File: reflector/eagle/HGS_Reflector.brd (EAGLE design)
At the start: 100 x 100 mm, 27 parts, among them J1 U.FL, U3 LP2985XX-N

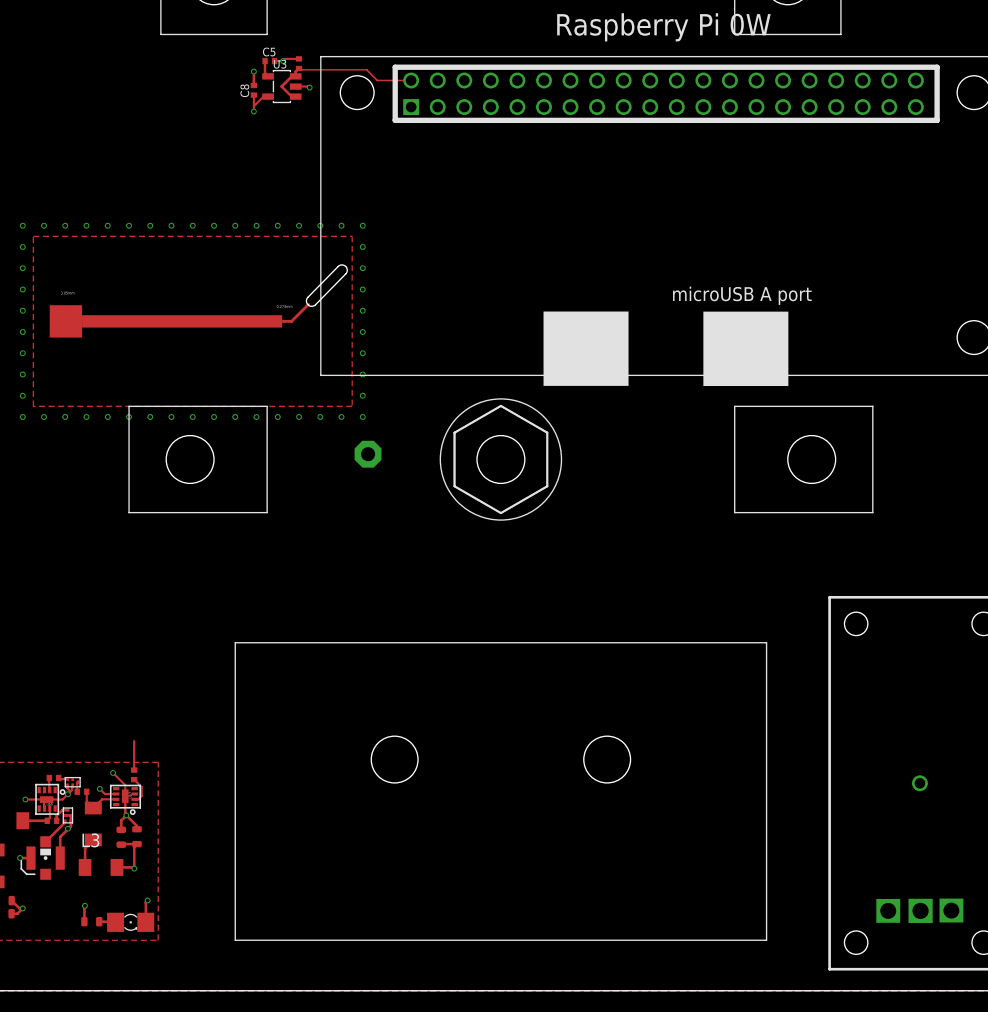
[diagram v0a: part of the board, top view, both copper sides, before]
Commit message: After connecting the Pi 0W footprint to the ground plane, I fixed the issue of the Pi 0W pin header floating.
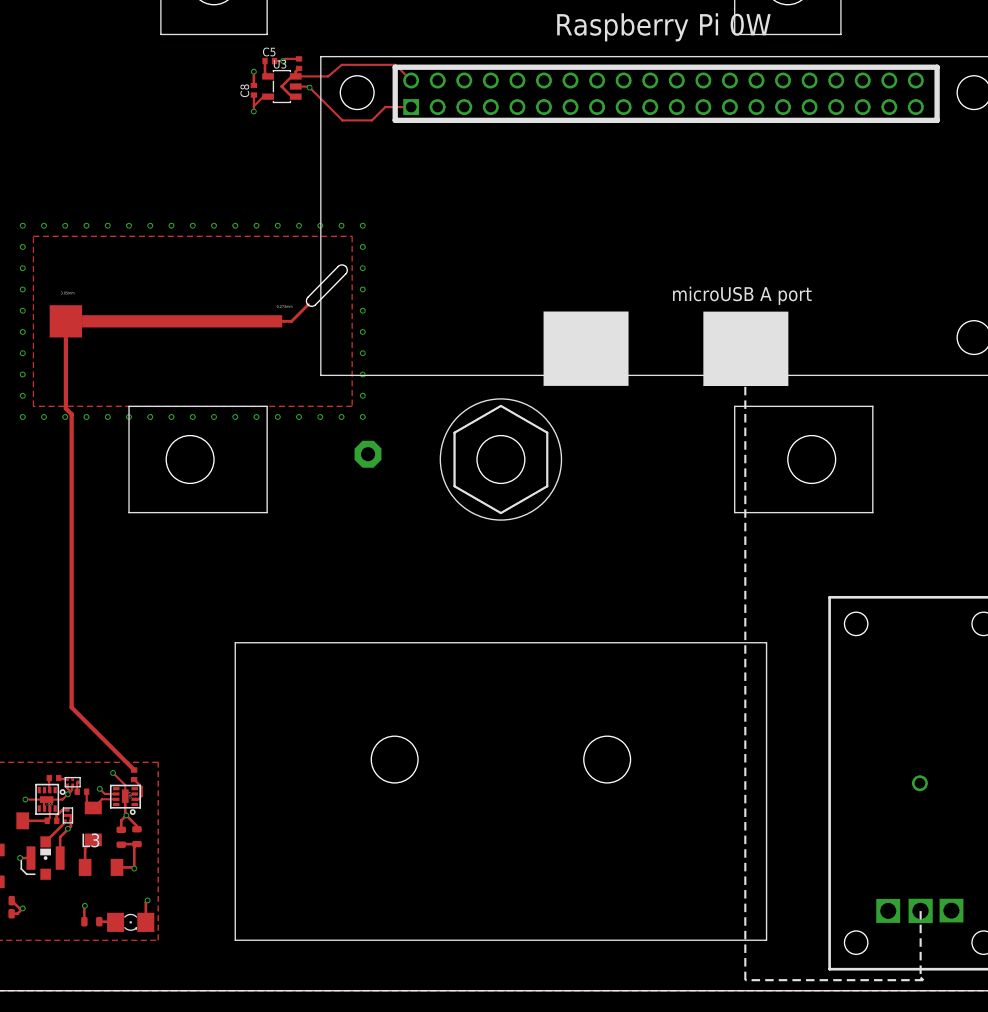
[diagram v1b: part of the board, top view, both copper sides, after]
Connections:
- net GND: now also U$5.GND
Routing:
- net N$9: track 2.73 -> 44.9 mm
- net GND: track 32.1 -> 43.5 mm
- net N$15: track 15.3 -> 16.2 mm

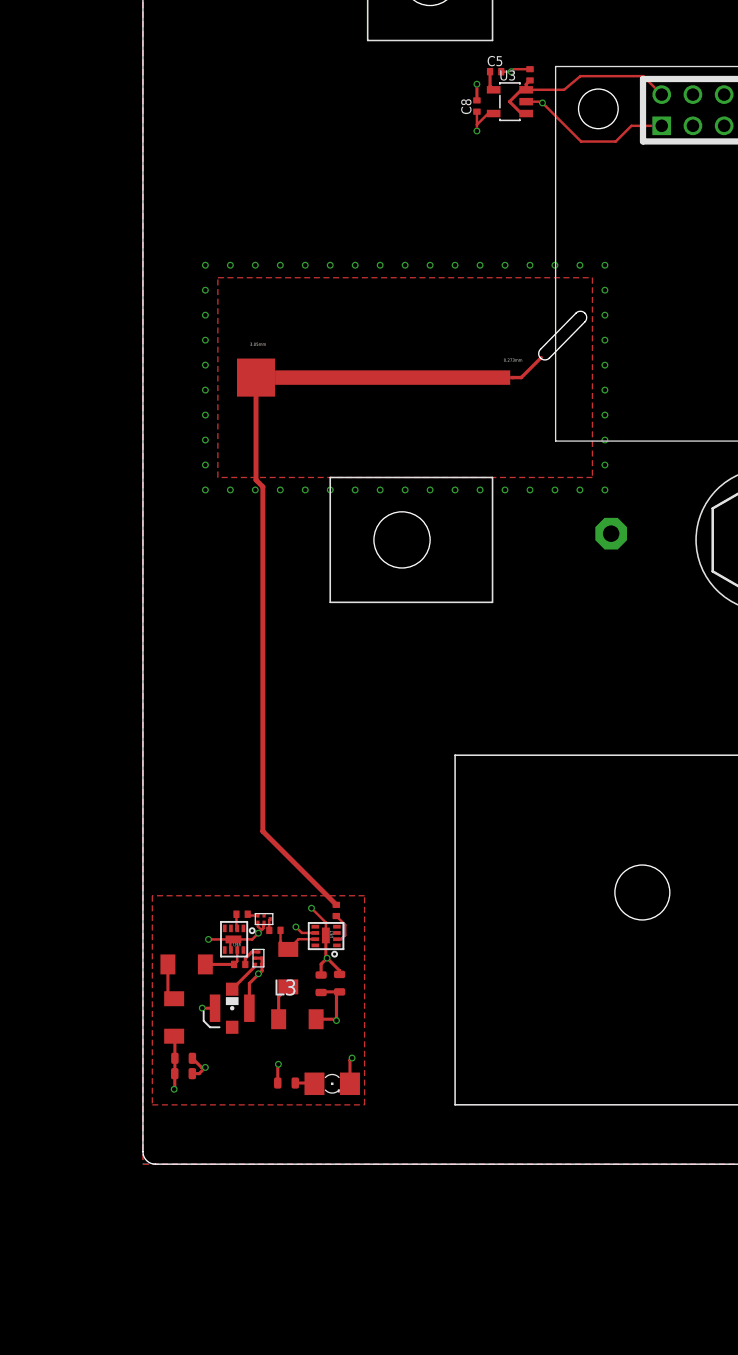
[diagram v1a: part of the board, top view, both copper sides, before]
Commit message: Design review of HGS - moving towards Oliver's power distribution ideas from 12/14.
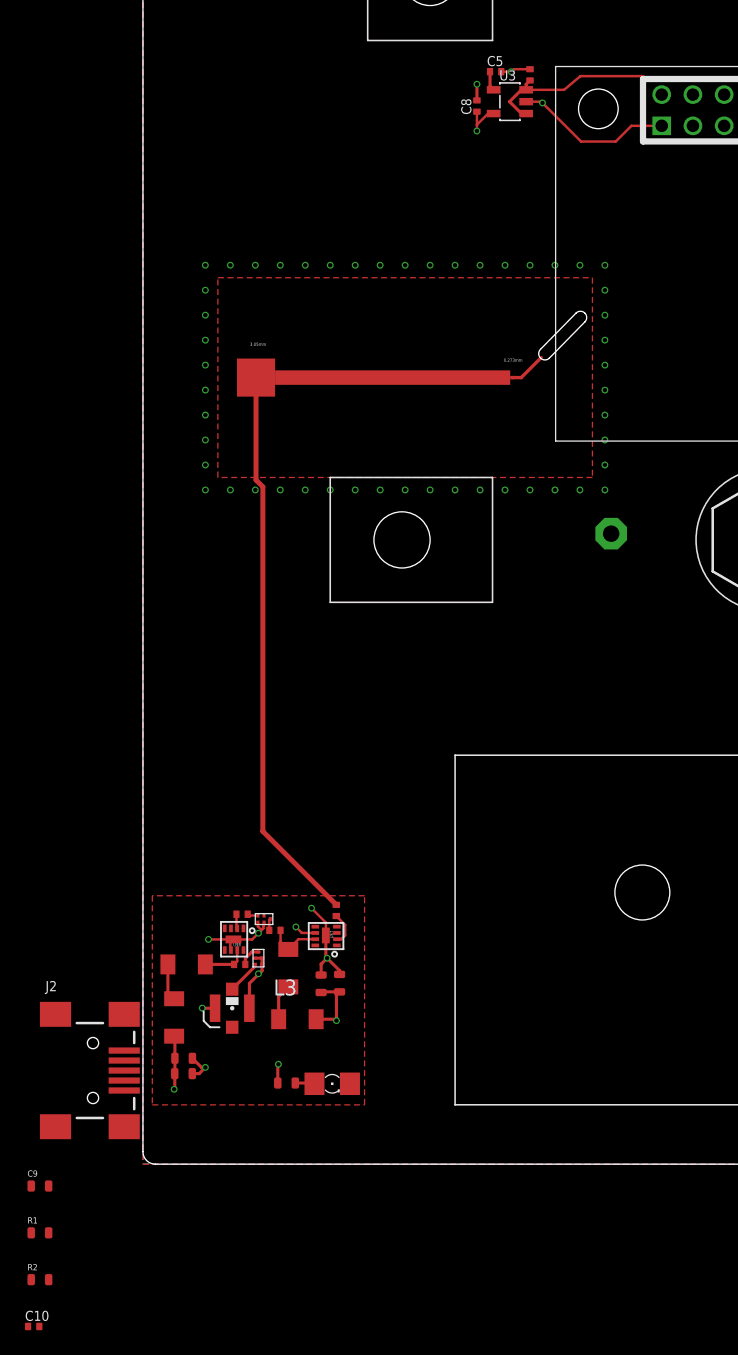
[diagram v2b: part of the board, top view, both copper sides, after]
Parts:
- added C10: 1 uF, oresat-rcl:.0402-C-NOSILK
- added C9: 100 pF, oresat-rcl:.0603-C-NOSILK
- added J2: USB_MINI-B_SMT, SparkFun-Connectors:USB-MINIB
- added R1, R2: FERRITE, oresat-rcl:.0603-C-NOSILK
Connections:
- new net N$12: C9.1, J2.S1, J2.S2, J2.S3, J2.S4
- new net N$17: J2.VBUS, R1.2
- new net N$18: R2.2
- new net VUSB: C10.2, C7.2, R1.1, R2.1, R9.2, U3.1, U3.3
- net 3.3V: no longer R9.2
- net GND: now also C10.1, C9.2, J2.GND
- net N$15: no longer C7.2, U3.1, U3.3
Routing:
- net N$15: track 16.2 -> 0.00 mm
- net VUSB: track 0.00 -> 15.6 mm, vias 0 -> 1
- net GND: track 43.5 -> 41.4 mm, vias 62 -> 61
- net 3.3V: track 14.7 -> 13.1 mm, vias 4 -> 3

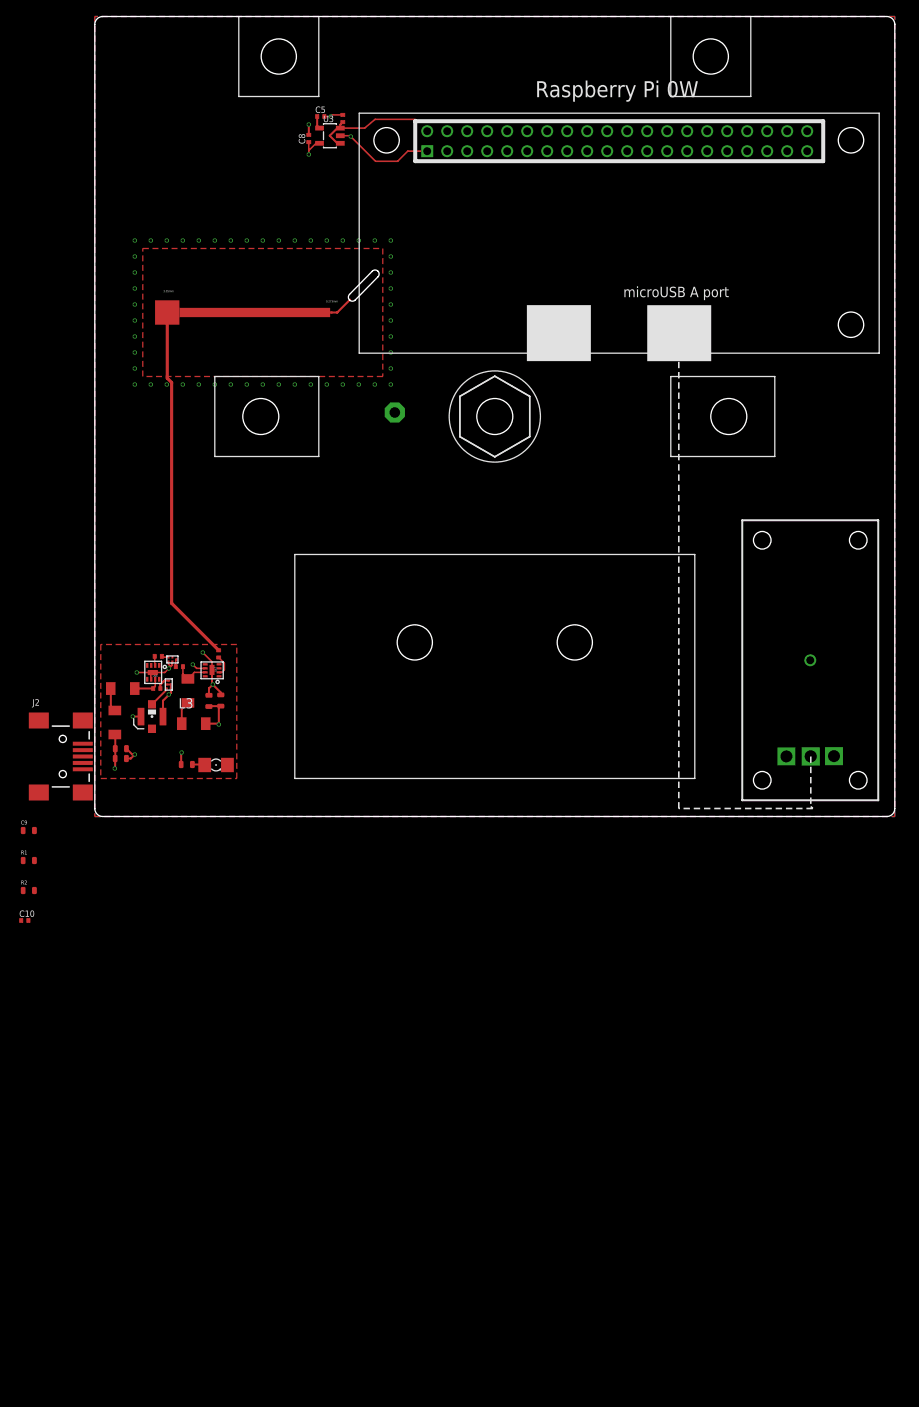
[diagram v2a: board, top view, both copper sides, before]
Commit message: After modifying the schematic symbol in the ferrite bead library, I updated the HGS schematic to match Oliver Jones' power distribution block diagram.
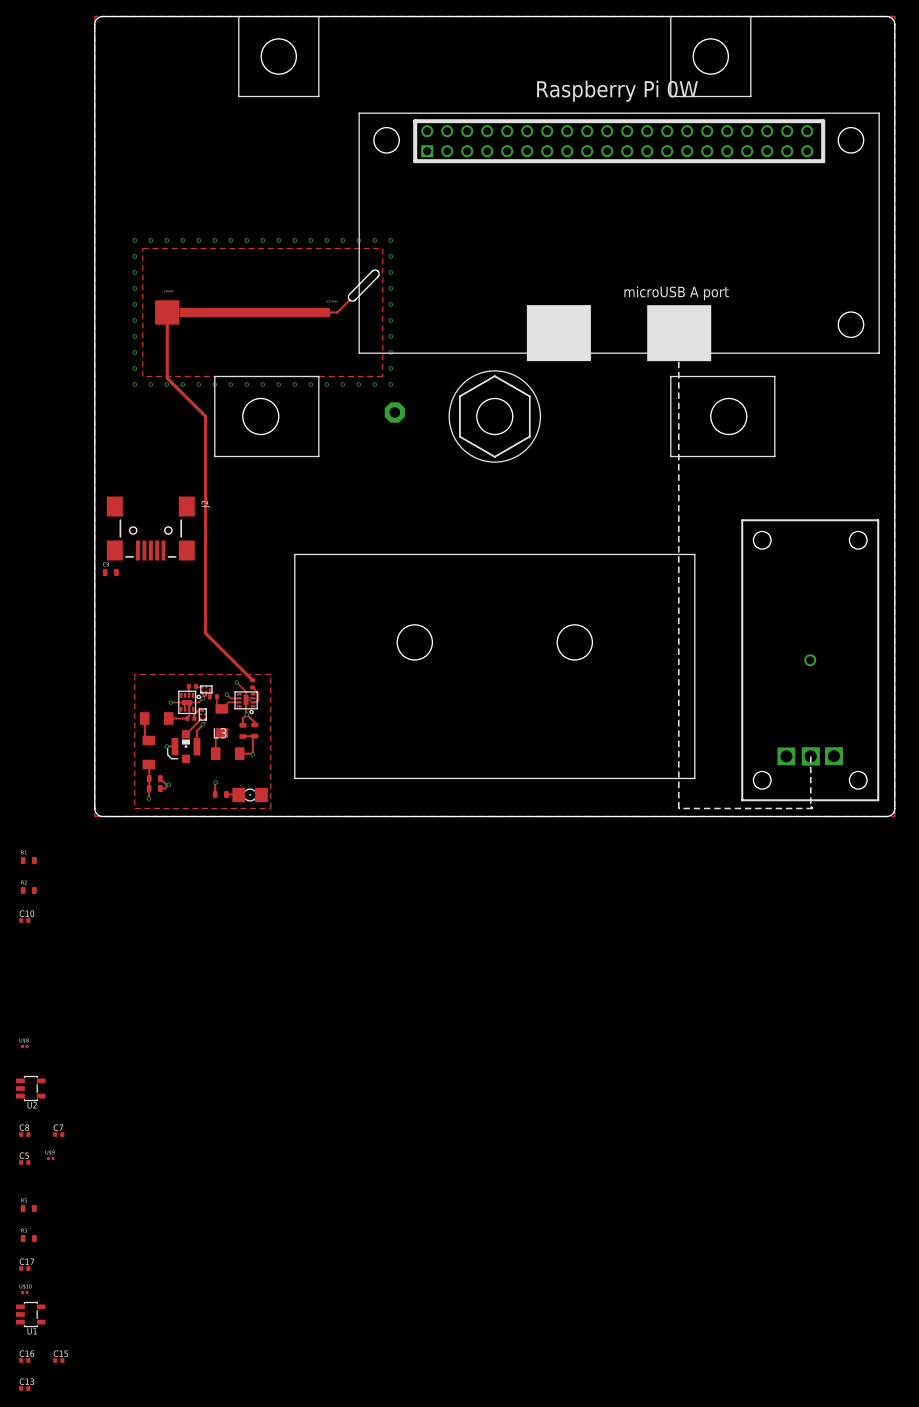
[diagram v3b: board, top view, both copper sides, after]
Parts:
- removed U3: LP2985XX-N, U-TI-LP2985XX-N-linear-reg:SOT-23
- added C13, C17: 1 uF, oresat-rcl:.0402-C-NOSILK
- added C15: 10 nF, oresat-rcl:.0402-C-NOSILK
- added C16: 2.2 uF, oresat-rcl:.0402-C-NOSILK
- added R3, R5: FERRITE, oresat-rcl:.0603-C-NOSILK
- added U$10, U$8, U$9: FERRITE_BEAD, Ferrite Bead:RESC0603X26N
- added U1, U2: LP2985XX-N, U-TI-LP2985XX-N-linear-reg:SOT-23
- C5: value 10 nF -> 1 uF
- C7: value 1 uF -> 10 nF
- moved C5 135.9 mm to (-8.75, -43.2)
- moved C7 131.9 mm to (-4.50, -39.8), turned to 0 degrees
- moved C8 129.5 mm to (-8.75, -39.8), turned to 0 degrees
- moved C9 33.8 mm to (2.00, 30.5)
- moved J2 30.3 mm to (7.00, 35.8), turned to 270 degrees
- moved C6 5.67 mm to (19.7, 16.6)
- moved L3 5.67 mm to (16.6, 7.86)
- moved LED1 5.67 mm to (19.4, 2.69)
- moved C1 5.67 mm to (7.50, 3.50)
- moved C11 5.67 mm to (20.0, 10.8)
- moved C12 5.67 mm to (18.5, 10.7)
- moved C14 5.67 mm to (14.8, 15.0)
- moved C2 5.67 mm to (7.51, 4.73)
- moved C3 5.67 mm to (12.2, 16.3)
- moved C4 5.67 mm to (12.0, 12.2)
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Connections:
- removed net 3.3V: C1.1, C11.1, C12.1, C2.1, C8.1, L3.2, L4.2, U3.5
- new net N$19: C15.1, U1.4
- new net N$20: C11.1, C12.1, L3.2, U$9.2
- new net N$21: C1.1, C2.1, L4.2, U$8.2
- new net N$22: C16.1, R5.1, U1.5
- new net N$25: C8.1, R3.1, U2.5
- net GND: now also C13.1, C15.2, C16.2, C17.1, C5.1, C7.2, C9.1, U1.2, U2.2; no longer C5.2, C7.1, C9.2, U3.2
- net N$1: now also C7.1, U2.4; no longer C5.1, U3.4
- net N$12: now also C9.2; no longer C9.1
- net N$15: now also C17.2, U$10.2
- net N$18: now also U$10.1
- net VUSB: now also C13.2, C5.2, U1.1, U1.3, U2.1, U2.3; no longer C7.2, U3.1, U3.3
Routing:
- net GND: track 41.4 -> 23.4 mm, vias 61 -> 58
- net VUSB: track 15.6 -> 1.52 mm
- net 3.3V: track 13.1 -> 0.00 mm, vias 3 -> 0
- net N$20: track 0.00 -> 5.58 mm, vias 0 -> 1
- net N$9: track 44.9 -> 50.4 mm
- net N$21: track 0.00 -> 4.30 mm, vias 0 -> 1
- net N$1: track 1.57 -> 0.00 mm
